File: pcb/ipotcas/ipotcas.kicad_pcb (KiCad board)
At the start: 4 copper layers, 71.1 x 94 mm, 74 parts, among them J1 Screw_Terminal_01x02, J10 Conn_01x03, J11 AudioJack4, J12 Conn_01x07, J13 Conn_01x03, J14 Conn_01x02, J2 Screw_Terminal_01x02, J3 Screw_Terminal_01x02, J4 Conn_01x06, J5 Barrel_Jack_Switch, J6 AudioJack4, J7 Conn_01x03, J8 Conn_01x03, J9 Conn_01x02, U1 NUCLEO144-F767ZI, U2 MCP602, U3 LM741, U4 TC7662Bx0A, Y1 SG-210STF

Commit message: Fix silkscreen labeling
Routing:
- net /LED_STATUS: track 3.24 -> 16.8 mm
- net /LED_ERR: track 3.24 -> 15.9 mm
- net GND: track 59.2 -> 61.1 mm
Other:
- board text added: "-12V"
- board text added: "ERR"
- board text added: "FROM PC"
- board text added: "PCIN"
- board text added: "QUIET"
- board text added: "RX"
- board text added: "STATUS"
- board text added: "TO HEADSET"

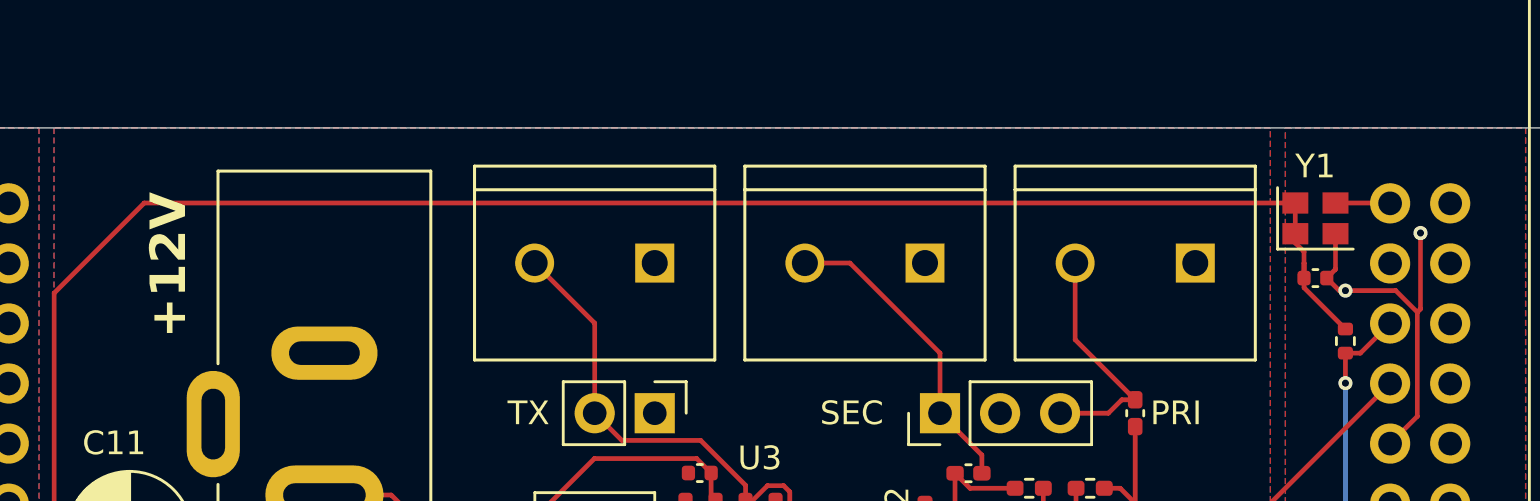
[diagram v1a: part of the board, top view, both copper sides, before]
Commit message: Fix clearance violation
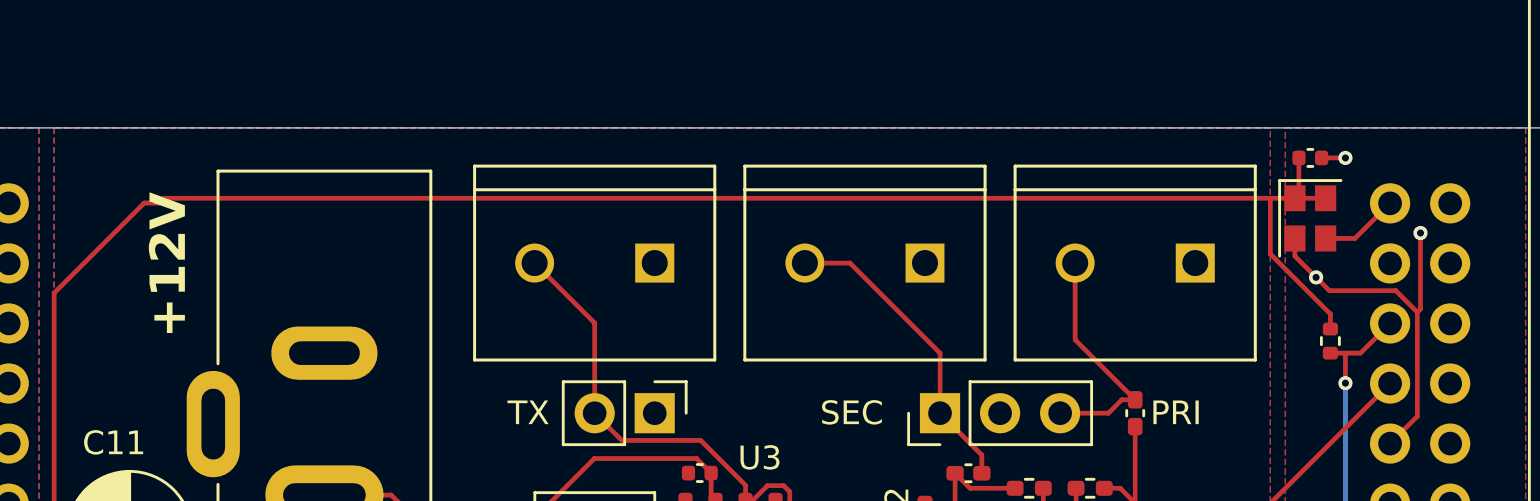
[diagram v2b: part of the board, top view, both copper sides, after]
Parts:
- moved C1 5.08 mm to (113.5, 62.2)
- moved R2 0.64 mm to (114.3, 70.0)
- moved Y1 0.22 mm to (113.5, 64.8), turned to -90 degrees
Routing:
- net +3.3V: track 145.1 -> 147.9 mm
- net GND: track 61.1 -> 62.6 mm, vias 20 -> 21
- net /AUDIO_CLK: track 2.32 -> 3.36 mm
- net /SDA: track 60.0 -> 60.7 mm
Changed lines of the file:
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@@
 	(footprint "Capacitor_SMD:C_0402_1005Metric"
 		(layer "F.Cu")
-		(at 113.665 67.31)
+		(at 113.45 62.23)
 		(descr "Capacitor SMD 0402 (1005 Metric), square (rectangular) end terminal, IPC_7351 nominal, (Body size source: IPC-SM-782 page 76, https://www.pcb-3d.com/wordpress/wp-content/uploads/ipc-sm-782a_amendment_1_and_2.pdf), generated with kicad-footprint-generator")
 		(tags "capacitor")
@@
 	(footprint "Resistor_SMD:R_0402_1005Metric"
 		(layer "F.Cu")
-		(at 114.935 69.975 -90)
+		(at 114.3 69.975 -90)
 		(descr "Resistor SMD 0402 (1005 Metric), square (rectangular) end terminal, IPC_7351 nominal, (Body size source: IPC-SM-782 page 72, https://www.pcb-3d.com/wordpress/wp-content/uploads/ipc-sm-782a_amendment_1_and_2.pdf), generated with kicad-footprint-generator")
 		(tags "resistor")
@@
 	(footprint "Oscillator:Oscillator_SMD_SeikoEpson_SG210-4Pin_2.5x2.0mm"
 		(layer "F.Cu")
-		(at 113.665 64.785)
+		(at 113.45 64.785 -90)
 		(descr "SMD Crystal Oscillator Seiko Epson SG-210 https://support.epson.biz/td/api/doc_check.php?mode=dl&lang=en&Parts=SG-210SED, 2.5x2.0mm^2 package")
 		(tags "SMD SMT crystal oscillator")
 		(property "Reference" "Y1"
-			(at 0 -2.2 0)
+			(at 3.19 0.85 90)
 			(layer "F.SilkS")
+			(hide yes)
 			(effects
 				(font
@@
 		)
 		(property "Value" "SG-210STF"
-			(at 0 2.2 0)
+			(at 0 2.2 90)
 			(layer "F.Fab")
 			(effects
@@
 		)
 		(property "Datasheet" "https://support.epson.biz/td/api/doc_check.php?mode=dl&lang=en&Parts=SG-210STF"
-			(at 0 0 0)
+			(at 0 0 270)
 			(unlocked yes)
 			(layer "F.Fab")
@@
 		)
 		(property "Description" "CMOS Crystal Oscillator SPXO"
-			(at 0 0 0)
+			(at 0 0 270)
 			(unlocked yes)
 			(layer "F.Fab")
@@
 		(attr smd)
 		(fp_line
-			(start -1.6 -1.3)
-			(end -1.6 1.3)
+			(start -1.6 1.3)
+			(end 1.6 1.3)
 			(stroke
 				(width 0.12)
@@
 		)
 		(fp_line
-			(start -1.6 1.3)
-			(end 1.6 1.3)
+			(start -1.6 -1.3)
+			(end -1.6 1.3)
 			(stroke
 				(width 0.12)
@@
 		)
 		(fp_line
-			(start -1.7 -1.4)
-			(end -1.7 1.4)
+			(start -1.7 1.4)
+			(end 1.7 1.4)
 			(stroke
 				(width 0.05)
@@
 		)
 		(fp_line
-			(start -1.7 1.4)
-			(end 1.7 1.4)
+			(start 1.7 1.4)
+			(end 1.7 -1.4)
 			(stroke
 				(width 0.05)
@@
 		)
 		(fp_line
-			(start 1.7 -1.4)
-			(end -1.7 -1.4)
+			(start -1.7 -1.4)
+			(end -1.7 1.4)
 			(stroke
 				(width 0.05)
@@
 		)
 		(fp_line
-			(start 1.7 1.4)
-			(end 1.7 -1.4)
+			(start 1.7 -1.4)
+			(end -1.7 -1.4)
 			(stroke
 				(width 0.05)
@@
 		)
 		(fp_line
-			(start -1.25 -1)
-			(end -1.25 1)
+			(start -1.25 1)
+			(end 1.25 1)
 			(stroke
 				(width 0.1)
@@
 		)
 		(fp_line
-			(start -1.25 0)
-			(end -0.25 1)
+			(start 1.25 1)
+			(end 1.25 -1)
 			(stroke
 				(width 0.1)
@@
 		)
 		(fp_line
-			(start -1.25 1)
-			(end 1.25 1)
+			(start -1.25 0)
+			(end -0.25 1)
 			(stroke
 				(width 0.1)
@@
 		)
 		(fp_line
-			(start 1.25 -1)
-			(end -1.25 -1)
+			(start -1.25 -1)
+			(end -1.25 1)
 			(stroke
 				(width 0.1)
@@
 		)
 		(fp_line
-			(start 1.25 1)
-			(end 1.25 -1)
+			(start 1.25 -1)
+			(end -1.25 -1)
 			(stroke
 				(width 0.1)
@@
 		)
 		(fp_text user "${REFERENCE}"
-			(at 0 0 0)
+			(at 0 0 90)
 			(layer "F.Fab")
 			(effects
@@
 		)
 		(pad "1" smd rect
-			(at -0.85 0.65)
+			(at -0.85 0.65 270)
 			(size 1.1 0.9)
 			(layers "F.Cu" "F.Mask" "F.Paste")
@@
 		)
 		(pad "2" smd rect
-			(at 0.85 0.65)
+			(at 0.85 0.65 270)
 			(size 1.1 0.9)
 			(layers "F.Cu" "F.Mask" "F.Paste")
@@
 		)
 		(pad "3" smd rect
-			(at 0.85 -0.65)
+			(at 0.85 -0.65 270)
 			(size 1.1 0.9)
 			(layers "F.Cu" "F.Mask" "F.Paste")
@@
 		)
 		(pad "4" smd rect
-			(at -0.85 -0.65)
+			(at -0.85 -0.65 270)
 			(size 1.1 0.9)
 			(layers "F.Cu" "F.Mask" "F.Paste")
@@
 	)
 	(segment
-		(start 114.515 66.94)
-		(end 114.145 67.31)
-		(width 0.2)
-		(layer "F.Cu")
-		(net 107)
-	)
-	(segment
-		(start 117.06376 67.841)
-		(end 114.935 67.841)
-		(width 0.2)
-		(layer "F.Cu")
-		(net 107)
-	)
-	(segment
 		(start 118.11 68.61924)
 		(end 118.11 65.405)
@@
 	)
 	(segment
-		(start 114.676 67.841)
-		(end 114.145 67.31)
+		(start 113.93 62.23)
+		(end 114.935 62.23)
 		(width 0.2)
 		(layer "F.Cu")
@@
 	)
 	(segment
-		(start 117.976 68.75324)
-		(end 117.06376 67.841)
-		(width 0.2)
-		(layer "F.Cu")
-		(net 107)
-	)
-	(segment
 		(start 92.7 82.06)
 		(end 92.7 80.655)
@@
 	)
 	(segment
+		(start 117.976 68.75324)
+		(end 117.06376 67.841)
+		(width 0.2)
+		(layer "F.Cu")
+		(net 107)
+	)
+	(segment
 		(start 92.0225 95.9875)
 		(end 92.0225 95.9375)
@@
 	)
 	(segment
-		(start 114.515 65.435)
-		(end 114.515 66.94)
+		(start 113.695 67.28)
+		(end 112.8 66.385)
 		(width 0.2)
 		(layer "F.Cu")
@@
 	)
 	(segment
-		(start 114.935 67.841)
-		(end 114.676 67.841)
+		(start 117.06376 67.841)
+		(end 114.256 67.841)
 		(width 0.2)
 		(layer "F.Cu")
@@
 	)
 	(segment
+		(start 112.8 66.385)
+		(end 112.8 65.635)
+		(width 0.2)
+		(layer "F.Cu")
+		(net 107)
+	)
+	(segment
 		(start 92.075 92.71)
 		(end 92.71 92.075)
@@
 	)
 	(segment
+		(start 114.256 67.841)
+		(end 113.695 67.28)
+		(width 0.2)
+		(layer "F.Cu")
+		(net 107)
+	)
+	(segment
 		(start 87.640003 93.5)
 		(end 87.63 93.510003)
@@
 	)
 	(via
-		(at 114.935 67.841)
+		(at 110.49 102.235)
 		(size 0.6)
 		(drill 0.3)
 		(layers "F.Cu" "B.Cu")
+		(free yes)
 		(net 107)
 	)
 	(via
-		(at 110.49 102.235)
+		(at 113.695 67.28)
 		(size 0.6)
 		(drill 0.3)
 		(layers "F.Cu" "B.Cu")
-		(free yes)
 		(net 107)
 	)
@@
 	)
 	(via
+		(at 114.935 62.23)
+		(size 0.6)
+		(drill 0.3)
+		(layers "F.Cu" "B.Cu")
+		(net 107)
+	)
+	(via
 		(at 74.295 86.36)
 		(size 0.6)
@@
 	)
 	(segment
+		(start 112.97 62.23)
+		(end 112.97 63.765)
+		(width 0.2)
+		(layer "F.Cu")
+		(net 108)
+	)
+	(segment
 		(start 60.325 80.01)
 		(end 58.405 81.93)
@@
 	)
 	(segment
-		(start 113.185 67.715)
-		(end 114.935 69.465)
+		(start 114.3 68.83)
+		(end 114.3 69.465)
 		(width 0.2)
 		(layer "F.Cu")
@@
 	)
 	(segment
-		(start 112.815 65.825)
-		(end 113.185 66.195)
+		(start 111.76 63.935)
+		(end 111.76 66.29)
 		(width 0.2)
 		(layer "F.Cu")
@@
 	)
 	(segment
-		(start 113.185 66.195)
-		(end 113.185 66.675)
+		(start 111.76 66.29)
+		(end 114.3 68.83)
 		(width 0.2)
 		(layer "F.Cu")
@@
 	)
 	(segment
-		(start 113.185 66.675)
-		(end 113.185 67.715)
+		(start 111.76 63.935)
+		(end 112.8 63.935)
 		(width 0.2)
 		(layer "F.Cu")
@@
 	)
 	(segment
-		(start 83.289 103.401)
-		(end 83.82 102.87)
+		(start 64.77 64.135)
+		(end 64.97 63.935)
 		(width 0.2)
 		(layer "F.Cu")
@@
 	)
 	(segment
-		(start 83.82 102.05466)
-		(end 83.82 102.87)
+		(start 114.1 63.935)
+		(end 112.8 63.935)
 		(width 0.2)
 		(layer "F.Cu")
@@
 	)
 	(segment
-		(start 113.185 66.675)
-		(end 113.185 67.31)
+		(start 83.289 103.401)
+		(end 83.82 102.87)
 		(width 0.2)
 		(layer "F.Cu")
@@
 	)
 	(segment
-		(start 112.815 65.435)
-		(end 112.815 65.825)
+		(start 83.82 102.05466)
+		(end 83.82 102.87)
 		(width 0.2)
 		(layer "F.Cu")
@@
 	)
 	(segment
+		(start 64.97 63.935)
+		(end 111.76 63.935)
+		(width 0.2)
+		(layer "F.Cu")
+		(net 108)
+	)
+	(segment
 		(start 85.99066 99.884)
 		(end 83.82 102.05466)
@@
 	)
 	(segment
-		(start 112.815 64.135)
-		(end 112.815 65.435)
+		(start 112.97 63.765)
+		(end 112.8 63.935)
 		(width 0.2)
 		(layer "F.Cu")
@@
 	)
 	(segment
-		(start 112.815 64.135)
-		(end 64.135 64.135)
+		(start 64.135 64.135)
+		(end 64.77 64.135)
 		(width 0.2)
 		(layer "F.Cu")
@@
 	)
 	(segment
+		(start 114.3 70.485)
+		(end 114.935 70.485)
+		(width 0.2)
+		(layer "F.Cu")
+		(net 142)
+	)
+	(segment
 		(start 114.935 70.485)
 		(end 115.57 70.485)
@@
 	)
 	(segment
-		(start 114.515 64.135)
-		(end 116.81 64.135)
+		(start 116.81 64.135)
+		(end 116.825 64.15)
 		(width 0.2)
 		(layer "F.Cu")
@@
 	)
 	(segment
-		(start 116.81 64.135)
+		(start 115.34 65.635)
 		(end 116.825 64.15)
 		(width 0.2)
 		(layer "F.Cu")
+		(net 145)
+	)
+	(segment
+		(start 114.1 65.635)
+		(end 115.34 65.635)
+		(width 0.2)
+		(layer "F.Cu")

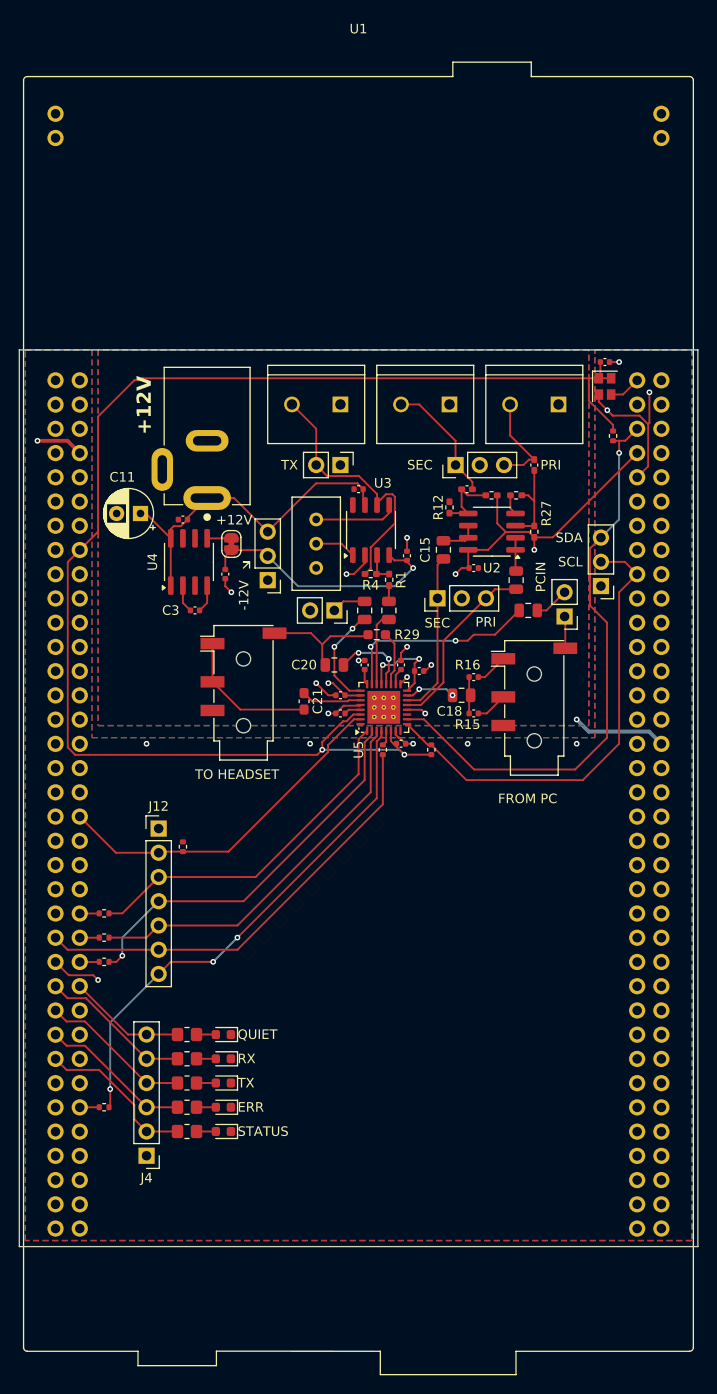
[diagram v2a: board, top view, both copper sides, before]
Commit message: Port RX to new PCB
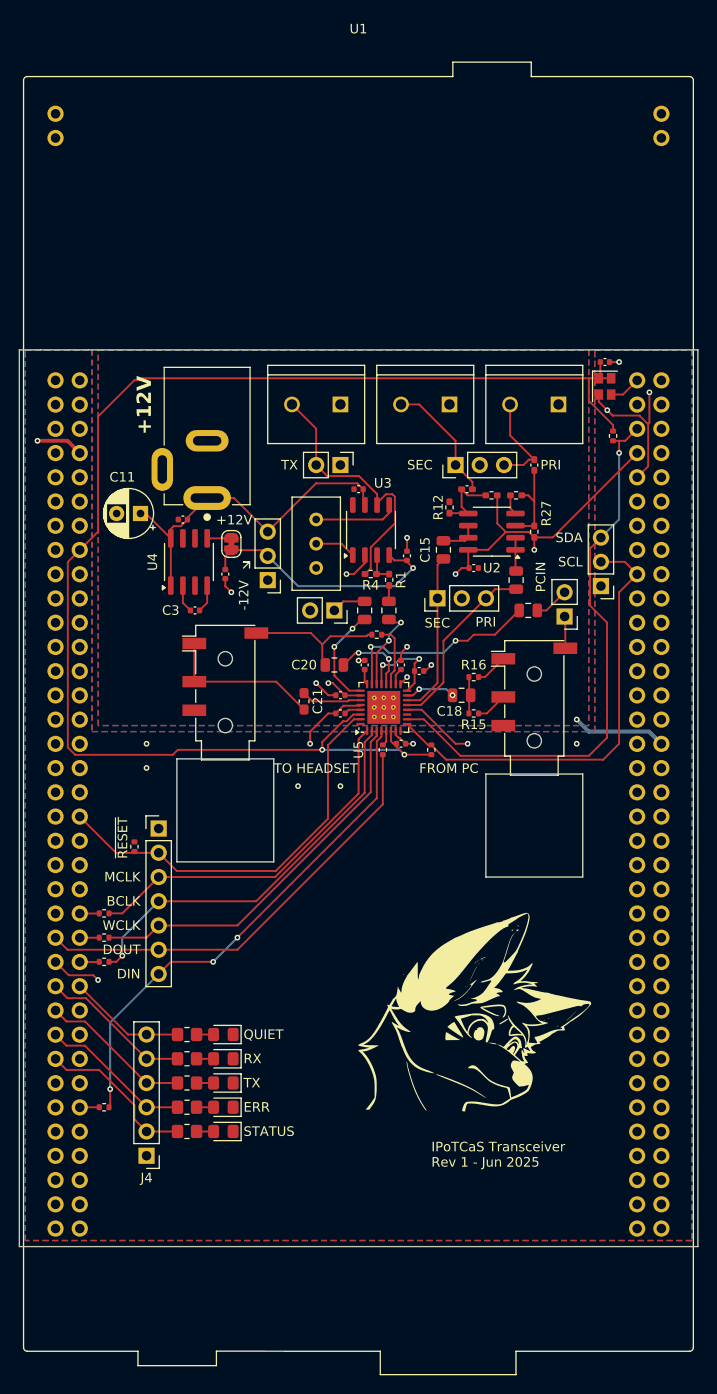
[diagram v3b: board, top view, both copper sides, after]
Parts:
- added G***: LOGO, Careers:salixwhat_1in, F.Cu at (99.7, 130.2)
- D1, D2, D3, D4, D5: footprint LED_SMD:LED_0603_1608Metric -> LED_SMD:LED_0805_2012Metric_Pad1.15x1.40mm_HandSolder
- R15, R16: footprint Capacitor_SMD:C_0402_1005Metric -> Resistor_SMD:R_0402_1005Metric
- R29: footprint Resistor_SMD:R_0603_1608Metric_Pad0.98x0.95mm_HandSolder -> Resistor_SMD:R_0402_1005Metric
- moved R28 5.08 mm to (64.1, 113.0)
- moved J11 1.91 mm to (73.7, 95.6)
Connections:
- C10 pad 2: GND -> GNDA
- C11 pad 2: GND -> GNDA
- C12 pad 2: GND -> GNDA
- C19 pad 2: GND -> GNDA
- C2 pad 2: GND -> GNDA
- C22 pad 2: GND -> GNDA
- C4 pad 2: GND -> GNDA
- C5 pad 2: GND -> GNDA
- C8 pad 2: GND -> GNDA
- C9 pad 2: GND -> GNDA
- J1 pad 1: GND -> GNDA
- J10 pad 1: GND -> GNDA
- J11 pad R2: GND -> GNDA
- J14 pad 2: GND -> GNDA
- J2 pad 1: GND -> GNDA
- J3 pad 1: GND -> GNDA
- J5 pad 2: GND -> GNDA
- J6 pad R2: GND -> GNDA
- J7 pad 2: GND -> GNDA
- J8 pad 2: GND -> GNDA
- J9 pad 1: GND -> GNDA
- R10 pad 2: GND -> GNDA
- R12 pad 2: GND -> GNDA
- U1 pad 104: GND -> GNDA
- U2 pad 4: GND -> GNDA
- U3 pad 2: GND -> GNDA
- U4 pad 3: GND -> GNDA
- U5 pad 17: GND -> GNDA
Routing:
- net GNDA: track 0.00 -> 25.7 mm, vias 0 -> 9
- net GND: track 62.6 -> 45.7 mm, vias 21 -> 13
- net /CODEC_~{RESET}: track 37.2 -> 43.7 mm
- net Net-(C20-Pad2): track 13.0 -> 15.3 mm
- net /HEADSET_OUT: track 14.8 -> 16.7 mm
- net /SCL: track 49.1 -> 47.3 mm
- net /CODEC_MCLK: track 37.1 -> 38.3 mm
- net /SDA: track 60.7 -> 59.5 mm
- net Net-(U5-LOL): track 7.73 -> 8.91 mm, vias 0 -> 2
- net /CODEC_BCLK: track 41.3 -> 42.1 mm
- net /MICBIAS: track 5.73 -> 6.48 mm
- net Net-(U5-LOR): track 21.1 -> 21.6 mm
- added copper zone on In2.Cu, net GND
- added copper zone on B.Cu, net GNDA
- added copper zone on F.Cu, net GNDA
- added copper zone on In1.Cu, net GNDA
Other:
- outline, holes or cut-outs redrawn
- board text added: "BCLK"
- board text added: "DIN"
- board text added: "DOUT"
- board text added: "IPoTCaS Transceiver Rev 1 - Jun 2025"
- board text added: "MCLK"
- board text added: "WCLK"
- board text added: "~{RESET}"
